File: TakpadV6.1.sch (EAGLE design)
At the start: 68 parts, among them J1 SD_CARD_SOCKET, J10 AUDIO_JACK_TRRSSMD_RA, J3 AVR_SPI_PROG_3X2PTH, T1 0, T2 0, T3 0, U1 ATMEGA328P_TQFP, U4 LM386N, Y1 20MHz

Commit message: Add files via upload
Minor Changes
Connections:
- net V+: now also U1.AVCC
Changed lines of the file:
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@@
 <?xml version="1.0" encoding="utf-8"?>
 <!DOCTYPE eagle SYSTEM "eagle.dtd">
-<eagle version="8.4.1">
+<eagle version="8.4.0">
 <drawing>
 <settings>
@@
 <setting verticaltext="up"/>
 </settings>
-<grid distance="0.1" unitdist="inch" unit="inch" style="lines" multiple="1" display="yes" altdistance="0.01" altunitdist="inch" altunit="inch"/>
+<grid distance="0.1" unitdist="inch" unit="inch" style="lines" multiple="1" display="no" altdistance="0.01" altunitdist="inch" altunit="inch"/>
 <layers>
 <layer number="1" name="Top" color="4" fill="1" visible="no" active="no"/>
@@
 <wire x1="-50.8" y1="17.78" x2="-66.04" y2="17.78" width="0.1524" layer="91"/>
 <wire x1="-66.04" y1="17.78" x2="-66.04" y2="20.32" width="0.1524" layer="91"/>
-<wire x1="-66.04" y1="27.94" x2="-66.04" y2="20.32" width="0.1524" layer="91"/>
+<wire x1="-66.04" y1="27.94" x2="-66.04" y2="22.86" width="0.1524" layer="91"/>
 <junction x="-66.04" y="20.32"/>
+<pinref part="U1" gate="U$1" pin="AVCC"/>
+<wire x1="-66.04" y1="22.86" x2="-66.04" y2="20.32" width="0.1524" layer="91"/>
+<wire x1="-50.8" y1="22.86" x2="-66.04" y2="22.86" width="0.1524" layer="91"/>
+<junction x="-66.04" y="22.86"/>
 </segment>
 <segment>

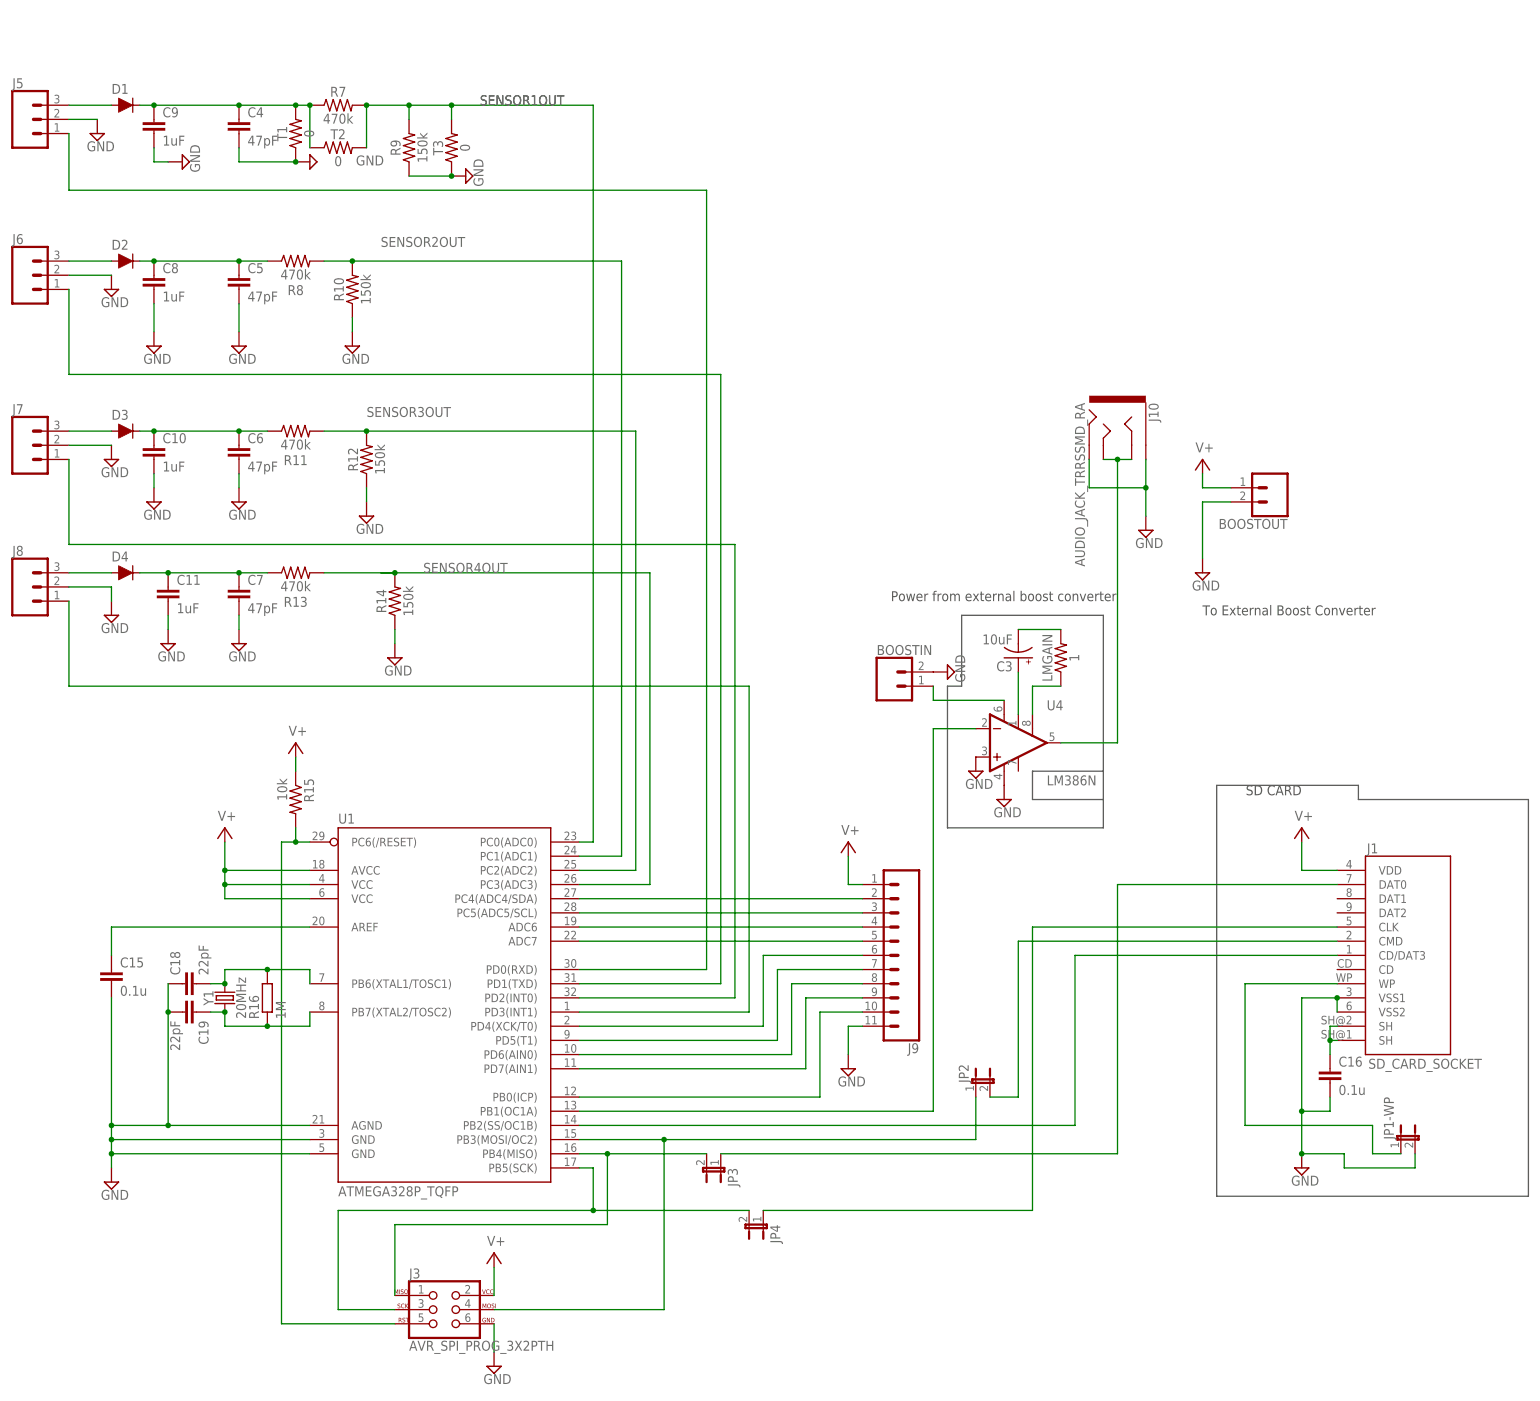
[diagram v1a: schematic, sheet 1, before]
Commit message: Add files via upload
added test points to voltage points of interest. Caps to input voltages, cap on output of lm386, smd resistors on inputs
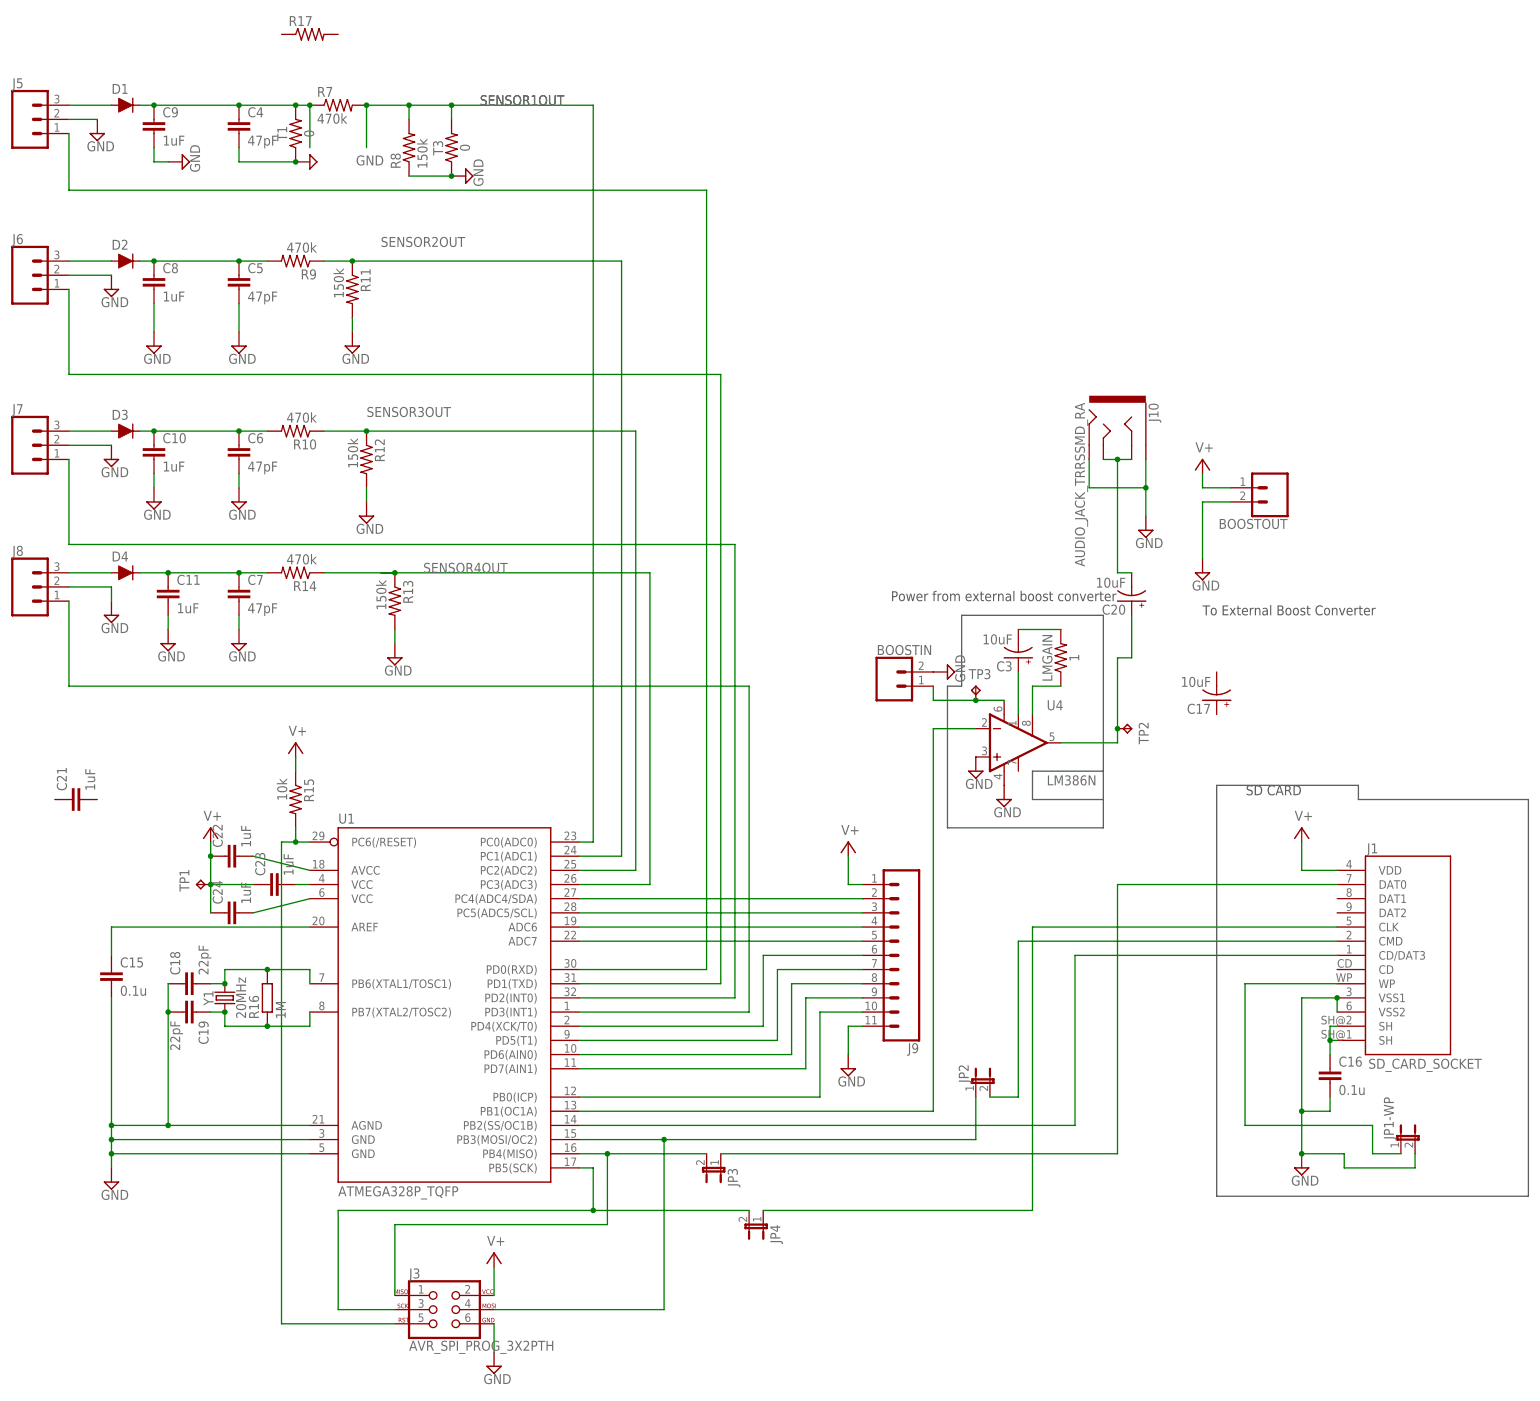
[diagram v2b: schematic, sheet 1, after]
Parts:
- removed T2: 0, SparkFun-Resistors:1KOHM-HORIZ-1/4W-1%
- added C17, C20: 10uF, SparkFun-Capacitors:10UF-POLAR-RADIAL-2.5MM-KIT-25V-20%
- added C21, C22, C23, C24: 1uF, SparkFun-Capacitors:47PF-0603-50V-5%
- added R17: (no value), rcl:R-US_M1206
- added TP1, TP2, TP3: TPPAD1-17, testpad:TPPAD1-17
- R10, R14, R9: value 150k -> 470k; device SparkFun-Resistors:1KOHM-HORIZ-1/4W-1% -> rcl:R-US_M1206
- R11, R13, R8: value 470k -> 150k; device SparkFun-Resistors:1KOHM-HORIZ-1/4W-1% -> rcl:R-US_M1206
- R12, R7: device SparkFun-Resistors:1KOHM-HORIZ-1/4W-1% -> rcl:R-US_M1206
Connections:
- new net N$1: C20.-, J10.RING1, J10.TIP
- new net N$2: C23.2, U1.VCC@4
- new net N$3: C22.2, U1.AVCC
- new net N$4: C24.2, U1.VCC@6
- net AUDIOOUT: now also C20.+, TP2.TP; no longer J10.RING1, J10.TIP
- net GND: now also R11.2, R12.2, R13.2, R8.1; no longer R10.1, R12.1, R14.1, R9.1
- net SENSOR1IN: no longer T2.1
- net SENSOR1OUT: now also R8.2; no longer R9.2, T2.2
- net SENSOR2IN: now also R9.2; no longer R8.1
- net SENSOR2OUT: now also R11.1, R9.1; no longer R10.2, R8.2
- net SENSOR3IN: now also R10.2; no longer R11.1
- net SENSOR3OUT: now also R10.1, R12.1; no longer R11.2, R12.2
- net SENSOR4IN: now also R14.2; no longer R13.1
- net SENSOR4OUT: now also R13.1, R14.1; no longer R13.2, R14.2
- net UPCONVERTERINPUT: now also TP3.TP
- net V+: now also C22.1, C23.1, C24.1, TP1.TP; no longer U1.AVCC, U1.VCC@4, U1.VCC@6
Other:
- moved on the sheet: R10, R11, R12, R13, R14, R8, R9
